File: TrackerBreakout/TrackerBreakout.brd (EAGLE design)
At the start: 17.8 x 22.9 mm, 15 parts

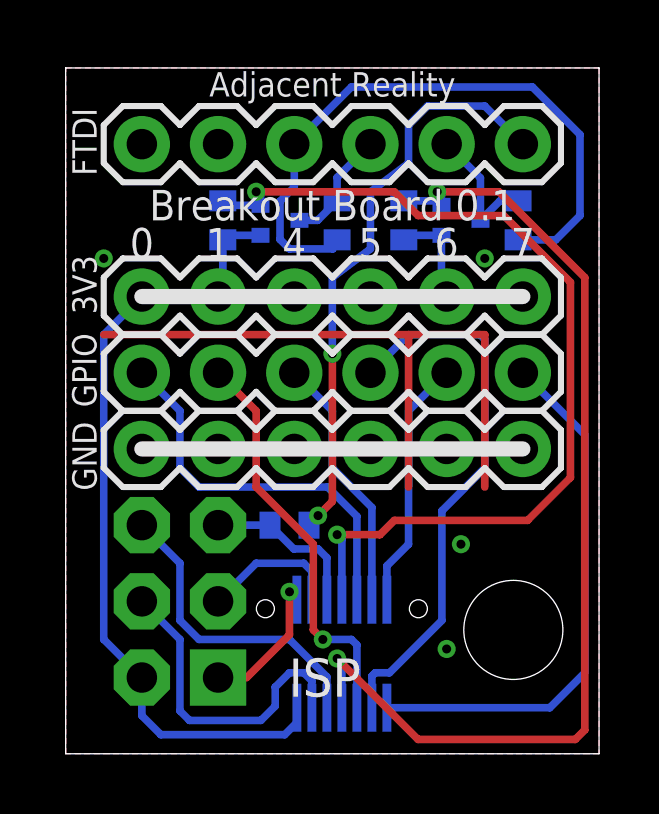
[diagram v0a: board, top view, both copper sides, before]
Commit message: fix connector direction
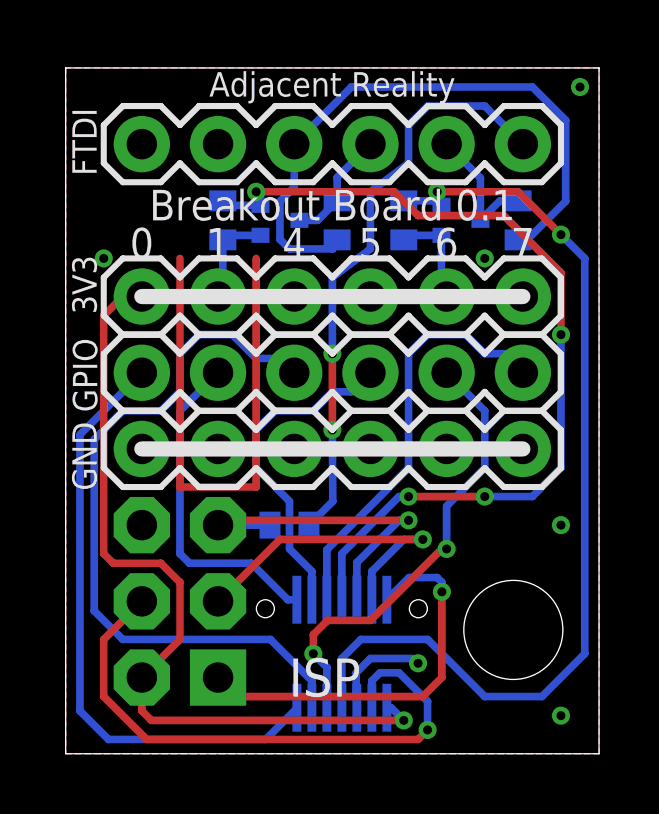
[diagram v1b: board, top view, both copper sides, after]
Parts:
- moved GPIO 12.7 mm to (15.2, 12.7), turned to 180 degrees
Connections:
- net +3V3: now also TRACKER.14; no longer TRACKER.2
- net GND: now also TRACKER.10; no longer TRACKER.6
- net N$1: now also TRACKER.5; no longer TRACKER.9
- net N$11: now also TRACKER.13; no longer TRACKER.1
- net N$2: now also TRACKER.6; no longer TRACKER.10
- net N$3: now also TRACKER.3; no longer TRACKER.11
- net N$4: now also TRACKER.4; no longer TRACKER.12
- net N$5: now also TRACKER.1; no longer TRACKER.13
- net N$6: now also TRACKER.2; no longer TRACKER.14
- net N$7: now also TRACKER.11; no longer TRACKER.3
- net N$9: now also TRACKER.12; no longer TRACKER.4
- net RESET: now also TRACKER.9; no longer TRACKER.5
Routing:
- net GND: track 33.3 -> 21.1 mm, vias 4 -> 6
- net N$9: track 10.7 -> 19.4 mm, vias 0 -> 1
- net N$11: track 4.77 -> 13.4 mm
- net RESET: track 5.48 -> 11.7 mm, vias 0 -> 1
- net N$7: track 4.71 -> 10.8 mm, vias 0 -> 1
- net +3V3: track 40.5 -> 46.2 mm, vias 0 -> 1
- net N$4: track 18.5 -> 24.2 mm
- net N$5: track 8.39 -> 11.1 mm
- net N$3: track 8.64 -> 11.0 mm
- net N$6: track 17.9 -> 20.2 mm
- net TX: track 34.2 -> 32.2 mm
- net N$2: track 13.6 -> 15.2 mm, vias 1 -> 2
- net RX: track 30.9 -> 29.6 mm, vias 2 -> 4
- net N$10: track 21.7 -> 20.7 mm
- net N$1: track 13.0 -> 13.9 mm

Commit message: so close
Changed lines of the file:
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@@
 <wire x1="17.78" y1="22.86" x2="0" y2="22.86" width="0" layer="20"/>
 <wire x1="0" y1="22.86" x2="0" y2="0" width="0" layer="20"/>
-<text x="2.54" y="16.51" size="1.016" layer="21" font="vector" align="bottom-center">0</text>
-<text x="5.08" y="16.51" size="1.016" layer="21" font="vector" align="bottom-center">1</text>
-<text x="7.62" y="16.51" size="1.016" layer="21" font="vector" align="bottom-center">4</text>
-<text x="10.16" y="16.51" size="1.016" layer="21" font="vector" align="bottom-center">5</text>
-<text x="12.7" y="16.51" size="1.016" layer="21" font="vector" align="bottom-center">6</text>
-<text x="15.24" y="16.51" size="1.016" layer="21" font="vector" align="bottom-center">7</text>
+<text x="15.24" y="16.51" size="1.016" layer="21" font="vector" align="bottom-center">0</text>
+<text x="12.7" y="16.51" size="1.016" layer="21" font="vector" align="bottom-center">1</text>
+<text x="10.16" y="16.51" size="1.016" layer="21" font="vector" align="bottom-center">4</text>
+<text x="7.62" y="16.51" size="1.016" layer="21" font="vector" align="bottom-center">5</text>
+<text x="5.08" y="16.51" size="1.016" layer="21" font="vector" align="bottom-center">6</text>
+<text x="2.54" y="16.51" size="1.016" layer="21" font="vector" align="bottom-center">7</text>
 <text x="8.89" y="21.9075" size="0.8128" layer="21" font="vector" align="bottom-center">Adjacent Reality</text>
 <text x="8.89" y="17.78" size="1.016" layer="21" font="vector" align="bottom-center">Breakout Board 0.1</text>
@@
 </signal>
 </signals>
-<errors>
-</errors>
 </board>
 </drawing>
